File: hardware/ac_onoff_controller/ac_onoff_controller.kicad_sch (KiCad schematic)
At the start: 41 parts, among them J1 Conn_02x04_Odd_Even, J2 Conn_01x02, M1 Motor_Servo, M2 Motor_Servo, Q1 2SK4017, Q2 2SK4017, Q3 2SC1815, Q6 2SK4017, SW1 SW_SPST, SW2 SW_Push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

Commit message: add a new pcb design for ordering to vendors
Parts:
- Q1, Q2, Q6: footprint ac_onoff_controller:2SK4017 -> Package_TO_SOT_THT:TO-251-3_Vertical
- R4, R5: footprint Resistor_THT:R_Axial_DIN0207_L6.3mm_D2.5mm_P2.54mm_Vertical -> Resistor_THT:R_Axial_DIN0309_L9.0mm_D3.2mm_P15.24mm_Horizontal
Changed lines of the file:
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@@
   )
   (symbol (lib_id "power:GND") (at 238.76 100.33 0) (unit 1)
-    (in_bom yes) (on_board yes) (dnp no) (fields_autoplaced)
+    (in_bom yes) (on_board yes) (dnp no)
     (property "Reference" "#PWR08" (at 238.76 106.68 0)
       (effects (font (size 1.27 1.27)) hide)
@@
       (effects (font (size 1.27 1.27)))
     )
-    (property "Footprint" "Resistor_THT:R_Axial_DIN0207_L6.3mm_D2.5mm_P2.54mm_Vertical" (at 220.98 99.568 90)
+    (property "Footprint" "Resistor_THT:R_Axial_DIN0309_L9.0mm_D3.2mm_P15.24mm_Horizontal" (at 220.98 99.568 90)
       (effects (font (size 1.27 1.27)) hide)
     )
@@
       (effects (font (size 1.27 1.27)) (justify left))
     )
-    (property "Footprint" "ac_onoff_controller:2SK4017" (at 284.48 113.03 0)
+    (property "Footprint" "Package_TO_SOT_THT:TO-251-3_Vertical" (at 284.48 113.03 0)
       (effects (font (size 1.27 1.27)) hide)
     )
@@
       (effects (font (size 1.27 1.27)))
     )
-    (property "Footprint" "Resistor_THT:R_Axial_DIN0207_L6.3mm_D2.5mm_P2.54mm_Vertical" (at 220.98 94.488 90)
+    (property "Footprint" "Resistor_THT:R_Axial_DIN0309_L9.0mm_D3.2mm_P15.24mm_Horizontal" (at 220.98 94.488 90)
       (effects (font (size 1.27 1.27)) hide)
     )
@@
   )
   (symbol (lib_id "power:VCC") (at 266.7 91.44 0) (unit 1)
-    (in_bom yes) (on_board yes) (dnp no) (fields_autoplaced)
+    (in_bom yes) (on_board yes) (dnp no)
     (property "Reference" "#PWR010" (at 266.7 95.25 0)
       (effects (font (size 1.27 1.27)) hide)
@@
       (effects (font (size 1.27 1.27)) (justify left))
     )
-    (property "Footprint" "ac_onoff_controller:2SK4017" (at 241.3 90.17 0)
+    (property "Footprint" "Package_TO_SOT_THT:TO-251-3_Vertical" (at 241.3 90.17 0)
       (effects (font (size 1.27 1.27)) hide)
     )
@@
   )
   (symbol (lib_id "Device:C") (at 228.6 81.28 0) (unit 1)
-    (in_bom yes) (on_board yes) (dnp no) (fields_autoplaced)
+    (in_bom yes) (on_board yes) (dnp no)
     (property "Reference" "C5" (at 232.41 80.01 0)
       (effects (font (size 1.27 1.27)) (justify left))
@@
       (effects (font (size 1.27 1.27)))
     )
-    (property "Footprint" "ac_onoff_controller:2SK4017" (at 76.2 38.1 0)
-      (effects (font (size 1.27 1.27)) hide)
-    )
+    (property "Footprint" "Package_TO_SOT_THT:TO-251-3_Vertical" (at 76.2 38.1 0)
+      (effects (font (size 1.27 1.27)) hide)
+    )

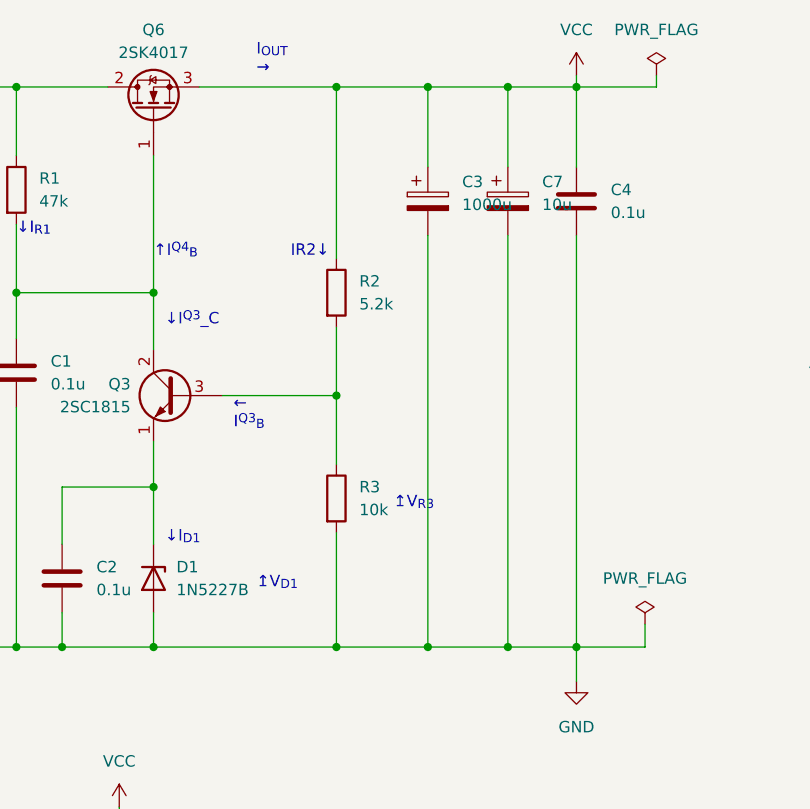
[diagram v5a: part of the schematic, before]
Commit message: use trim register for voltage regulator feedback
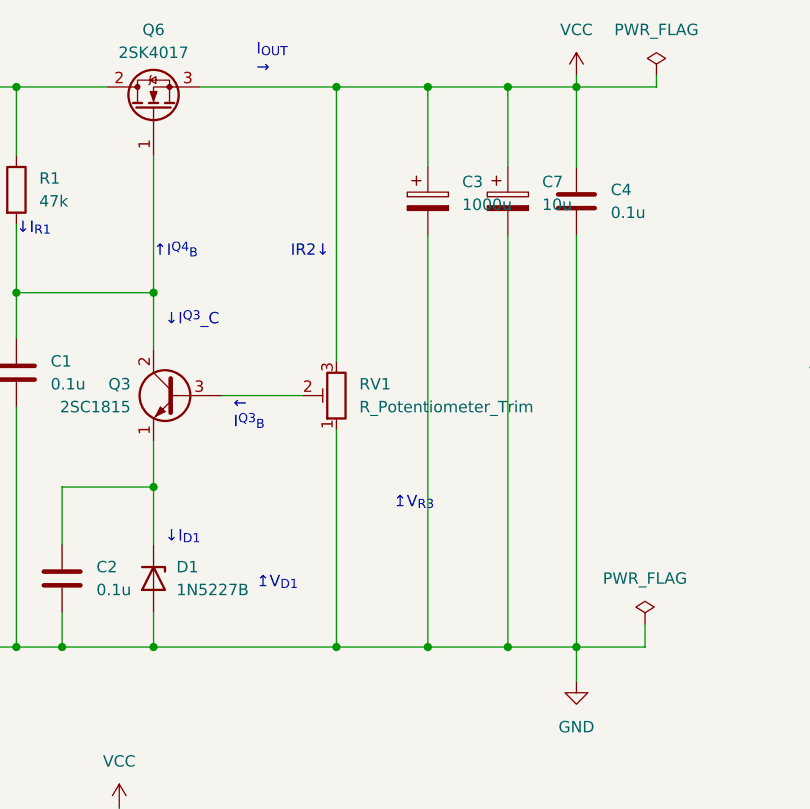
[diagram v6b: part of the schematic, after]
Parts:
- removed R2: 5.2k, Resistor_THT:R_Axial_DIN0309_L9.0mm_D3.2mm_P15.24mm_Horizontal, symbol Device:R
- removed R3: 10k, Resistor_THT:R_Axial_DIN0309_L9.0mm_D3.2mm_P15.24mm_Horizontal, symbol Device:R
- added RV1: R_Potentiometer_Trim, ac_onoff_controller:GF063P, symbol Device:R_Potentiometer_Trim
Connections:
- net GND: now also RV1.1
- net VCC: now also RV1.3
- net at Q3.3 (B): now also RV1.2

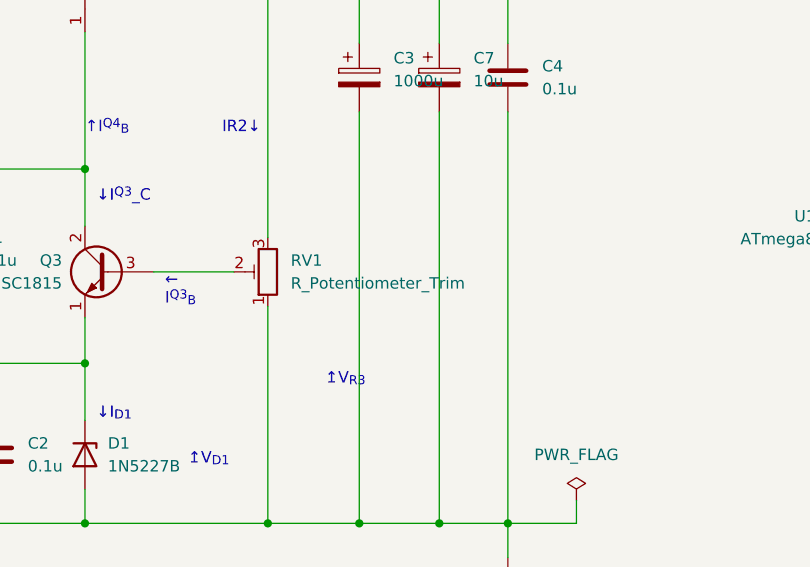
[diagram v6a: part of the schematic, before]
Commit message: add mpn of a trim register
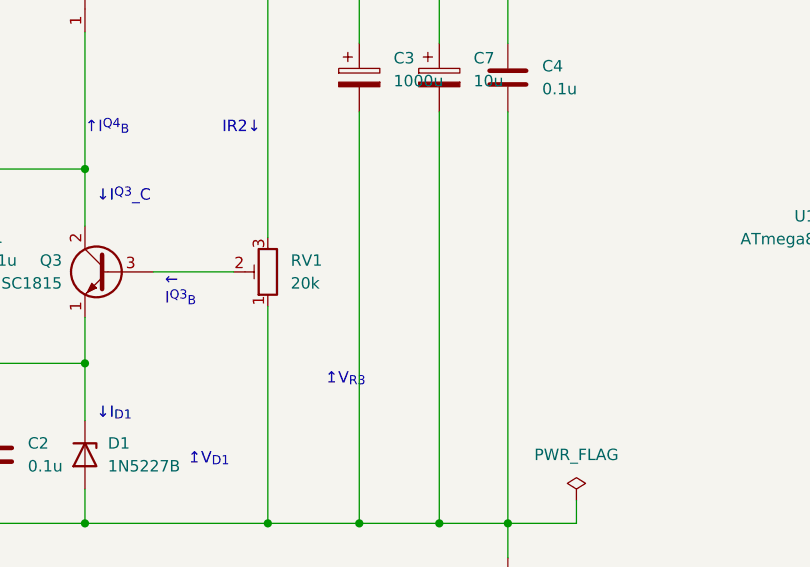
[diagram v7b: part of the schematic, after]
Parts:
- RV1: value R_Potentiometer_Trim -> 20k; URL (none) -> https://akizukidenshi.com/catalog/g/g114906/; note (none) -> purchase 100k, 50k and 10k at the same time.; purchase (none) -> 1
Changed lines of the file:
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@@
+      (effects (font (size 1.27 1.27)) hide)
+    )
+    (property "note" "" (at 273.05 142.24 0)
       (effects (font (size 1.27 1.27)) hide)
     )
@@
       (effects (font (size 1.27 1.27)) hide)
     )
+    (property "note" "" (at 252.73 118.11 0)
+      (effects (font (size 1.27 1.27)) hide)
+    )
     (pin "1")
     (pin "2")
@@
     )
     (property "Datasheet" "~" (at 67.31 185.42 0)
+      (effects (font (size 1.27 1.27)) hide)
+    )
+    (property "note" "" (at 67.31 185.42 0)
       (effects (font (size 1.27 1.27)) hide)
     )
@@
     )
     (property "purchase" "0" (at 181.61 102.87 0)
+      (effects (font (size 1.27 1.27)) hide)
+    )
+    (property "note" "" (at 181.61 102.87 0)
       (effects (font (size 1.27 1.27)) hide)
     )
@@
       (effects (font (size 1.27 1.27)) hide)
     )
+    (property "note" "" (at 63.5 72.39 0)
+      (effects (font (size 1.27 1.27)) hide)
+    )
     (pin "1")
     (pin "2")
@@
       (effects (font (size 1.27 1.27)) hide)
     )
+    (property "note" "" (at 78.74 95.25 0)
+      (effects (font (size 1.27 1.27)) hide)
+    )
     (pin "1")
     (pin "2")
@@
       (effects (font (size 1.27 1.27)) hide)
     )
+    (property "note" "" (at 193.04 163.83 0)
+      (effects (font (size 1.27 1.27)) hide)
+    )
     (pin "1")
     (pin "2")
@@
     )
     (property "purchase" "0" (at 222.25 148.59 0)
+      (effects (font (size 1.27 1.27)) hide)
+    )
+    (property "note" "" (at 222.25 148.59 0)
       (effects (font (size 1.27 1.27)) hide)
     )
@@
       (effects (font (size 1.27 1.27)) hide)
     )
+    (property "note" "" (at 220.98 97.79 0)
+      (effects (font (size 1.27 1.27)) hide)
+    )
     (pin "1")
     (pin "2")
@@
     )
     (property "purchase" "3" (at 279.4 115.57 0)
+      (effects (font (size 1.27 1.27)) hide)
+    )
+    (property "note" "" (at 279.4 115.57 0)
       (effects (font (size 1.27 1.27)) hide)
     )
@@
       (effects (font (size 1.27 1.27)) (justify right))
     )
-    (property "Value" "R_Potentiometer_Trim" (at 101.6 76.2 0)
+    (property "Value" "20k" (at 101.6 76.2 0)
       (effects (font (size 1.27 1.27)) (justify right))
     )
@@
       (effects (font (size 1.27 1.27)) hide)
     )
+    (property "Sim.Pins" "GF063P B203K" (at 99.06 74.93 0)
+      (effects (font (size 1.27 1.27)) hide)
+    )
+    (property "URL" "https://akizukidenshi.com/catalog/g/g114906/" (at 99.06 74.93 0)
+      (effects (font (size 1.27 1.27)) hide)
+    )
+    (property "note" "purchase 100k, 50k and 10k at the same time." (at 99.06 74.93 0)
+      (effects (font (size 1.27 1.27)) hide)
+    )
+    (property "purchase" "1" (at 99.06 74.93 0)
+      (effects (font (size 1.27 1.27)) hide)
+    )
     (pin "1")
     (pin "2")
@@
       (effects (font (size 1.27 1.27)) hide)
     )
+    (property "note" "" (at 48.26 40.64 0)
+      (effects (font (size 1.27 1.27)) hide)
+    )
     (pin "1")
     (pin "2")
@@
       (effects (font (size 1.27 1.27)) hide)
     )
+    (property "note" "" (at 220.98 92.71 0)
+      (effects (font (size 1.27 1.27)) hide)
+    )
     (pin "1")
     (pin "2")
@@
       (effects (font (size 1.27 1.27)) hide)
     )
+    (property "note" "" (at 289.56 99.06 0)
+      (effects (font (size 1.27 1.27)) hide)
+    )
     (pin "1")
     (pin "2")
@@
       (effects (font (size 1.27 1.27)) hide)
     )
+    (property "note" "" (at 262.89 142.24 0)
+      (effects (font (size 1.27 1.27)) hide)
+    )
     (pin "1")
     (pin "2")
@@
       (effects (font (size 1.27 1.27)) hide)
     )
+    (property "note" "" (at 125.73 53.34 0)
+      (effects (font (size 1.27 1.27)) hide)
+    )
     (pin "1")
     (pin "2")
@@
     )
     (property "purchase" "0" (at 254 142.24 0)
+      (effects (font (size 1.27 1.27)) hide)
+    )
+    (property "note" "" (at 254 142.24 0)
       (effects (font (size 1.27 1.27)) hide)
     )
@@
       (effects (font (size 1.27 1.27)) hide)
     )
+    (property "note" "" (at 273.05 153.67 0)
+      (effects (font (size 1.27 1.27)) hide)
+    )
     (pin "1")
     (pin "2")
@@
       (effects (font (size 1.27 1.27)) hide)
     )
+    (property "note" "" (at 68.58 95.25 0)
+      (effects (font (size 1.27 1.27)) hide)
+    )
     (pin "1")
     (pin "2")
@@
       (effects (font (size 1.27 1.27)) hide)
     )
+    (property "note" "" (at 63.5 52.07 0)
+      (effects (font (size 1.27 1.27)) hide)
+    )
     (pin "1")
     (pin "2")
@@
       (effects (font (size 1.27 1.27)) hide)
     )
+    (property "note" "" (at 271.78 102.87 0)
+      (effects (font (size 1.27 1.27)) hide)
+    )
     (pin "1")
     (pin "2")
@@
       (effects (font (size 1.27 1.27)) hide)
     )
+    (property "note" "" (at 213.36 81.28 0)
+      (effects (font (size 1.27 1.27)) hide)
+    )
     (pin "1")
     (pin "2")
@@
     )
     (property "purchase" "0" (at 163.83 163.83 0)
+      (effects (font (size 1.27 1.27)) hide)
+    )
+    (property "note" "" (at 163.83 163.83 0)
       (effects (font (size 1.27 1.27)) hide)
     )
@@
       (effects (font (size 1.27 1.27)) hide)
     )
+    (property "note" "" (at 109.22 53.34 0)
+      (effects (font (size 1.27 1.27)) hide)
+    )
     (pin "1")
     (pin "2")
@@
       (effects (font (size 1.27 1.27)) hide)
     )
+    (property "note" "" (at 74.93 138.43 0)
+      (effects (font (size 1.27 1.27)) hide)
+    )
     (pin "1")
     (pin "2")
@@
       (effects (font (size 1.27 1.27)) hide)
     )
+    (property "note" "" (at 118.11 53.34 0)
+      (effects (font (size 1.27 1.27)) hide)
+    )
     (pin "1")
     (pin "2")
@@
       (effects (font (size 1.27 1.27)) hide)
     )
+    (property "note" "" (at 254 153.67 0)
+      (effects (font (size 1.27 1.27)) hide)
+    )
     (pin "1")
     (pin "2")
@@
       (effects (font (size 1.27 1.27)) hide)
     )
+    (property "note" "" (at 236.22 92.71 0)
+      (effects (font (size 1.27 1.27)) hide)
+    )
     (pin "1")
     (pin "2")
@@
       (effects (font (size 1.27 1.27)) hide)
     )
+    (property "note" "" (at 67.31 190.5 0)
+      (effects (font (size 1.27 1.27)) hide)
+    )
     (instances
       (project "ac_onoff_controller"
@@
       (effects (font (size 1.27 1.27)) hide)
     )
+    (property "note" "" (at 251.46 77.47 0)
+      (effects (font (size 1.27 1.27)) hide)
+    )
     (pin "1")
     (pin "2")
@@
       (effects (font (size 1.27 1.27)) hide)
     )
+    (property "note" "" (at 67.31 175.26 0)
+      (effects (font (size 1.27 1.27)) hide)
+    )
     (instances
       (project "ac_onoff_controller"
@@
     )
     (property "purchase" "0" (at 34.29 45.72 0)
+      (effects (font (size 1.27 1.27)) hide)
+    )
+    (property "note" "" (at 34.29 45.72 0)
       (effects (font (size 1.27 1.27)) hide)
     )
@@
       (effects (font (size 1.27 1.27)) hide)
     )
+    (property "note" "" (at 67.31 180.34 0)
+      (effects (font (size 1.27 1.27)) hide)
+    )
     (instances
       (project "ac_onoff_controller"
@@
     )
     (property "purchase" "0" (at 208.28 163.83 0)
+      (effects (font (size 1.27 1.27)) hide)
+    )
+    (property "note" "" (at 208.28 163.83 0)
       (effects (font (size 1.27 1.27)) hide)
     )
@@
     )
     (property "purchase" "0" (at 262.89 153.67 0)
+      (effects (font (size 1.27 1.27)) hide)
+    )
+    (property "note" "" (at 262.89 153.67 0)
       (effects (font (size 1.27 1.27)) hide)
     )
@@
       (effects (font (size 1.27 1.27)) hide)
     )
+    (property "note" "" (at 228.6 81.28 0)
+      (effects (font (size 1.27 1.27)) hide)
+    )
     (pin "1")
     (pin "2")
@@
       (effects (font (size 1.27 1.27)) hide)
     )
+    (property "note" "" (at 256.54 102.87 0)
+      (effects (font (size 1.27 1.27)) hide)
+    )
     (pin "1")
     (pin "2")
@@
       (effects (font (size 1.27 1.27)) hide)
     )
+    (property "note" "" (at 78.74 43.18 0)
+      (effects (font (size 1.27 1.27)) hide)
+    )
     (pin "1")
     (pin "2")
@@
     )
     (property "purchase" "0" (at 177.8 163.83 0)
+      (effects (font (size 1.27 1.27)) hide)
+    )
+    (property "note" "" (at 177.8 163.83 0)
       (effects (font (size 1.27 1.27)) hide)
     )
@@
       (effects (font (size 1.27 1.27)) hide)
     )
+    (property "note" "" (at 81.28 74.93 0)
+      (effects (font (size 1.27 1.27)) hide)
+    )

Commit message: export gerbers for jlcpcb
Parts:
- added D7: D, Diode_THT:D_DO-15_P12.70mm_Horizontal, symbol Device:D
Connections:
- net VCC: now also D7.2 (A)
- net at C1.1, Q3.2 (C), Q6.1 (G)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: now also D7.1 (K)
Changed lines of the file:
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@@
   (junction (at 118.11 102.87) (diameter 0) (color 0 0 0 0)
+  )
+  (junction (at 99.06 53.34) (diameter 0) (color 0 0 0 0)
+  )
+  (junction (at 78.74 53.34) (diameter 0) (color 0 0 0 0)
   )
   (junction (at 63.5 63.5) (diameter 0) (color 0 0 0 0)
@@
     (stroke (width 0) (type default))
   )
+  (wire (pts (xy 99.06 53.34) (xy 99.06 71.12))
+    (stroke (width 0) (type default))
+  )
   (wire (pts (xy 228.6 85.09) (xy 238.76 85.09))
     (stroke (width 0) (type default))
@@
     (stroke (width 0) (type default))
   )
+  (wire (pts (xy 92.71 53.34) (xy 99.06 53.34))
+    (stroke (width 0) (type default))
+  )
   (wire (pts (xy 223.52 69.85) (xy 223.52 77.47))
     (stroke (width 0) (type default))
@@
     (stroke (width 0) (type default))
   )
-  (wire (pts (xy 78.74 48.26) (xy 78.74 63.5))
+  (wire (pts (xy 78.74 48.26) (xy 78.74 53.34))
     (stroke (width 0) (type default))
   )
@@
     (stroke (width 0) (type default))
   )
+  (wire (pts (xy 78.74 53.34) (xy 85.09 53.34))
+    (stroke (width 0) (type default))
+  )
   (wire (pts (xy 118.11 40.64) (xy 118.11 49.53))
     (stroke (width 0) (type default))
@@
     (stroke (width 0) (type default))
   )
-  (wire (pts (xy 99.06 40.64) (xy 99.06 71.12))
+  (wire (pts (xy 99.06 40.64) (xy 99.06 53.34))
     (stroke (width 0) (type default))
   )
@@
   )
   (wire (pts (xy 213.36 77.47) (xy 223.52 77.47))
+    (stroke (width 0) (type default))
+  )
+  (wire (pts (xy 78.74 53.34) (xy 78.74 63.5))
     (stroke (width 0) (type default))
   )
@@
         )
       )
+    )
+  )
+  (symbol (lib_id "Device:D") (at 88.9 53.34 0) (unit 1)
+    (in_bom yes) (on_board yes) (dnp no) (fields_autoplaced)
+    (property "Reference" "D7" (at 88.9 46.99 0)
+      (effects (font (size 1.27 1.27)))
+    )
+    (property "Value" "D" (at 88.9 49.53 0)
+      (effects (font (size 1.27 1.27)))
+    )
+    (property "Footprint" "Diode_THT:D_DO-15_P12.70mm_Horizontal" (at 88.9 53.34 0)
+      (effects (font (size 1.27 1.27)) hide)
+    )
+    (property "Datasheet" "~" (at 88.9 53.34 0)
+      (effects (font (size 1.27 1.27)) hide)
+    )
+    (property "Sim.Device" "D" (at 88.9 53.34 0)
+      (effects (font (size 1.27 1.27)) hide)
+    )
+    (property "Sim.Pins" "1=K 2=A" (at 88.9 53.34 0)
+      (effects (font (size 1.27 1.27)) hide)
+    )
+    (pin "1")
+    (pin "2")
+    (instances
+      (project "ac_onoff_controller"
+        (path "/3fdcfeb5-507b-4398-9c86-207e73e94441"
+          (reference "D7") (unit 1)
+        )
+      )
